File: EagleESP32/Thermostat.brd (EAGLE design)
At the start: 42.2 x 49.3 mm, 61 parts, among them K1 AQY282EHA, K2 AQY282EHA, K3 AQY282EHA, K4 AQY282EHA, K5 AQY282EHA, Q1 MOSFET-NCHANNELAO3404A, U1 ESP-WROOM-03, X1 1751303

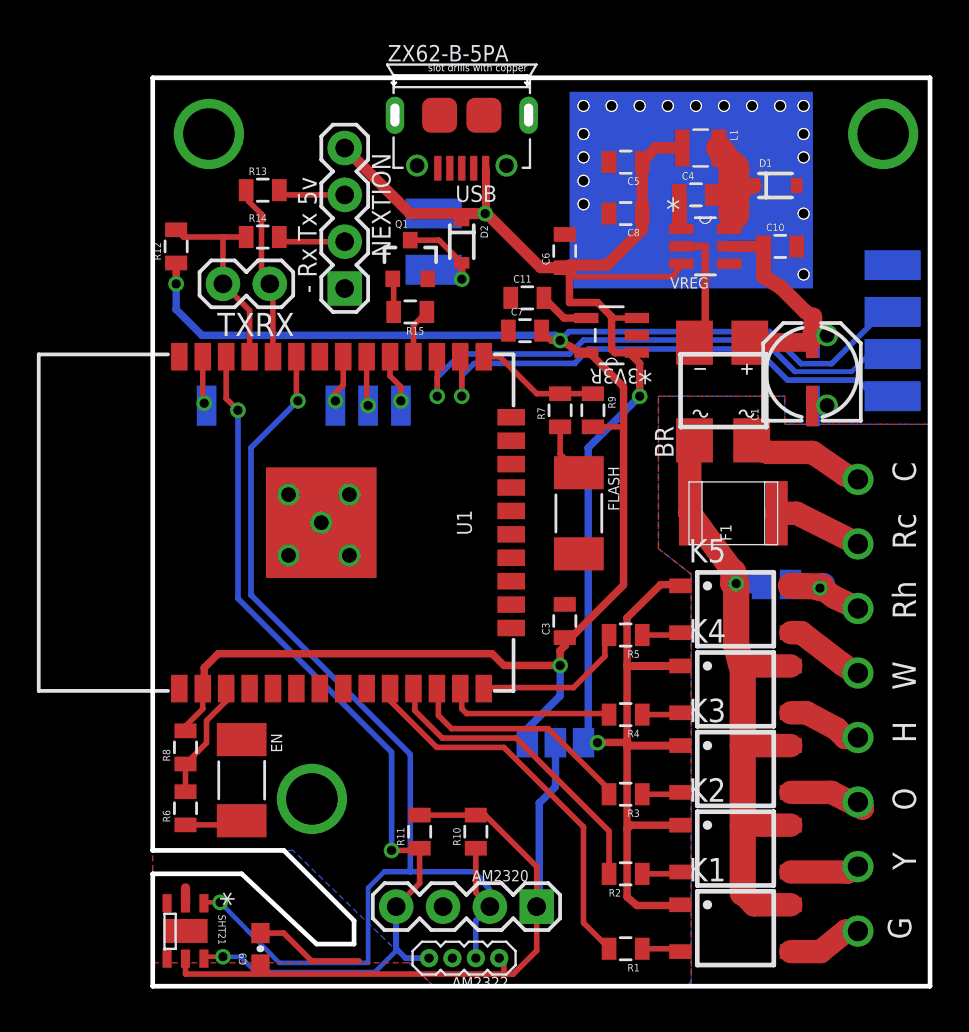
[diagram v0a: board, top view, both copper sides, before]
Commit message: rev 1. GPIO12 is connected to 1.3V LDO (r0 failed!)
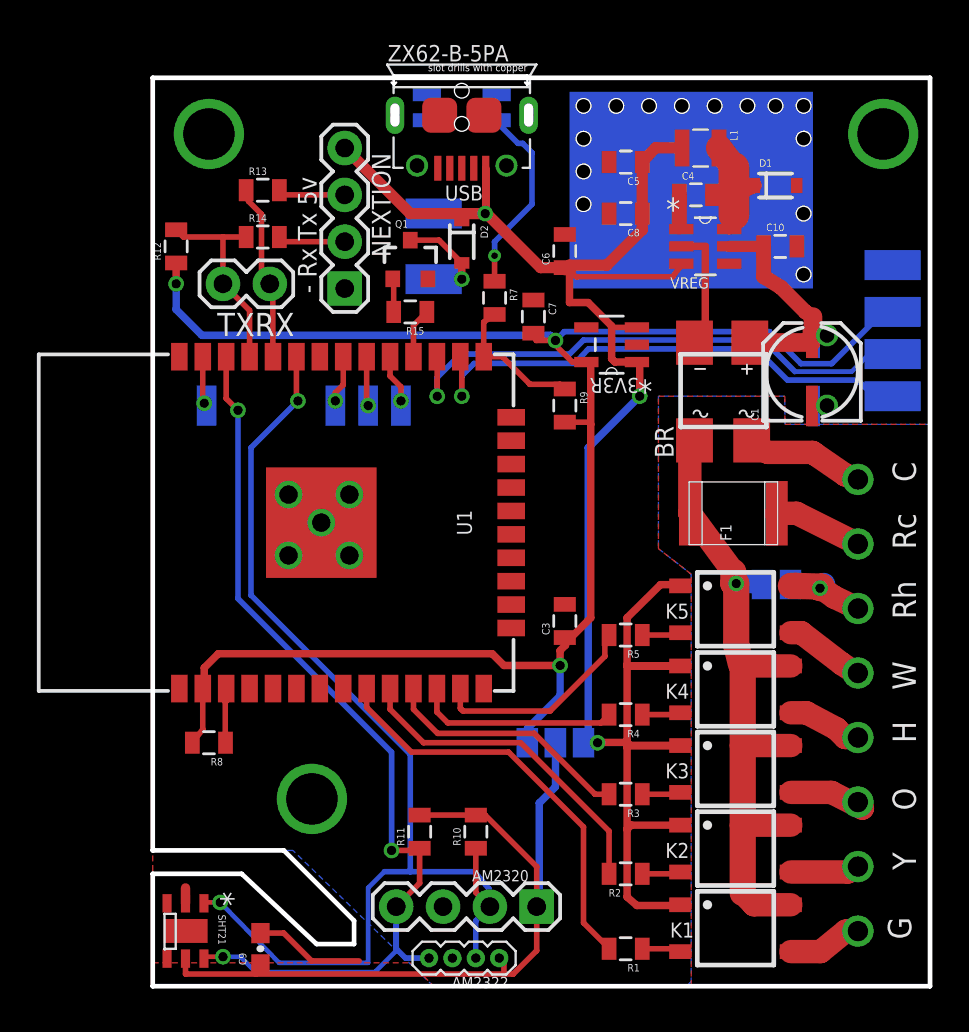
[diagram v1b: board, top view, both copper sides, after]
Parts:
- removed C11: (no value), SparkFun-Capacitors:0805
- removed EN, FLASH: BTN_4MM, CuriousTech:BTN_4MM
- removed R6: 470, SparkFun-Resistors:0805
- added U$6: SIDE-TACT, CuriousTech:SIDE-TACT
- K1, K2, K3, K4, K5: value AQY282EHA -> G3VM-61GR2
- moved R7 7.06 mm to (18.5, 37.3), turned to 270 degrees
- moved R9 1.55 mm to (22.4, 31.5)
- moved R8 1.30 mm to (3.05, 13.2), turned to 180 degrees
- moved C7 0.89 mm to (20.7, 36.3), turned to 270 degrees
- moved U$11 0.51 mm to (15.2, 38.4)
- moved 3V3R 0.51 mm to (24.9, 34.8)
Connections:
- removed net N$28: EN.2, R6.1
- removed net N$34: 3V3R.4, C11.2
- new net N$35: U1.24
- new net N$36: U1.16
- new net N$37: U1.23
- new net N$40: U1.8
- new net N$42: U1.6
- new net N$43: U1.7
- new net _NC: U1.32
- net COOL: now also U1.10; no longer U1.11
- net FAN: now also U1.9; no longer U1.10
- net GND: now also U$6.3, U$6.4; no longer C11.1, EN.1, FLASH.2
- net HEAT: now also U1.13; no longer U1.14
- net HUMID: now also U1.12; no longer U1.13
- net N$27: now also U$6.2; no longer FLASH.1
- net N$9: no longer R6.2
- net REV: now also U1.11; no longer U1.12
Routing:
- net N$27: track 2.91 -> 10.5 mm, vias 0 -> 1
- net N$9: track 6.51 -> 2.97 mm
- net N$28: track 3.14 -> 0.00 mm
- net HEAT: track 8.54 -> 11.5 mm
- net N$34: track 2.75 -> 0.00 mm
- net HUMID: track 9.25 -> 11.0 mm
- net FAN: track 21.2 -> 22.6 mm
- net COOL: track 16.8 -> 18.1 mm
- net N$14: track 6.75 -> 7.73 mm
- net REV: track 12.7 -> 13.6 mm
- net 5V: track 113.3 -> 112.6 mm
- net 3V3: track 96.9 -> 96.2 mm

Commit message: Worst mistake ever. I quit.
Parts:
- removed C2: 100uF, SparkFun-Capacitors:PANASONIC_C
- R14: value 5K6 -> 5K1
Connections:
- net 3V3: now also K1.1, K2.1, K3.1, K4.1, K5.1
- net 5V: no longer K1.1, K2.1, K3.1, K4.1, K5.1
- net GND: no longer C2.-
- net N$24: no longer C2.+
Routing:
- net 5V: track 112.6 -> 74.0 mm, vias 3 -> 2
- net 3V3: track 96.2 -> 129.7 mm
- net N$24: track 13.5 -> 12.7 mm
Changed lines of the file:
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@@
 <attribute name="VALUE" x="30.353" y="38.8874" size="2.0828" layer="27" ratio="10" rot="SR180"/>
 </element>
-<element name="R14" library="SparkFun-Resistors" package="0805" value="5K6" x="5.969" y="40.64" smashed="yes">
+<element name="R14" library="SparkFun-Resistors" package="0805" value="5K1" x="5.969" y="40.64" smashed="yes">
 <attribute name="NAME" x="5.207" y="41.4655" size="0.4064" layer="25"/>
 <attribute name="VALUE" x="4.953" y="39.243" size="0.4064" layer="27"/>
@@
 <attribute name="NAME" x="27.239" y="30.387" size="1.016" layer="25" ratio="10" rot="R270"/>
 <attribute name="VALUE" x="25.803" y="36.733" size="1.778" layer="27" ratio="10" rot="R270"/>
-</element>
-<element name="C2" library="SparkFun-Capacitors" package="PANASONIC_C" value="100uF" x="36.068" y="33.274" smashed="yes" rot="MR90">
-<attribute name="NAME" x="38.768" y="30.674" size="0.4064" layer="26" rot="MR90"/>
-<attribute name="VALUE" x="32.618" y="30.674" size="0.4064" layer="28" rot="MR90"/>
 </element>
 <element name="AM2320" library="SparkFun-Connectors" package="1X04" value="AM2320" x="20.828" y="4.318" smashed="yes" rot="R180">
@@
 <contactref element="C6" pad="2"/>
 <contactref element="BR" pad="-"/>
-<contactref element="C2" pad="-"/>
 <via x="36.576" y="31.496" extent="1-16" drill="0.8"/>
 <contactref element="AM2320" pad="3"/>
@@
 <wire x1="35.814" y1="36.322" x2="35.414178125" y2="36.570134375" width="0.8128" layer="1"/>
 <wire x1="35.414178125" y1="36.570134375" x2="34.07518125" y2="37.90913125" width="0.8128" layer="1"/>
-<contactref element="C2" pad="+"/>
 <wire x1="34.07518125" y1="37.90913125" x2="33.136" y2="38.492" width="0.8128" layer="1"/>
-<wire x1="36.576" y1="35.306" x2="36.444" y2="35.174" width="0.4064" layer="16"/>
-<wire x1="35.868" y1="35.174" x2="36.444" y2="35.174" width="0.4064" layer="16"/>
 <via x="36.576" y="35.306" extent="1-16" drill="0.8"/>
 <wire x1="36.576" y1="35.306" x2="36.4852875" y2="35.5781375" width="0.4064" layer="1"/>
@@
 <wire x1="22.352" y1="18.912" x2="22.393046875" y2="18.870953125" width="0.4064" layer="1"/>
 <wire x1="22.393046875" y1="18.870953125" x2="22.393046875" y2="18.500953125" width="0.4064" layer="1"/>
-<wire x1="23.76" y1="19.98230625" x2="23.76" y2="30.48" width="0.4064" layer="1"/>
+<wire x1="23.76" y1="19.98230625" x2="23.76" y2="20.447" width="0.4064" layer="1"/>
 <wire x1="23.76" y1="30.48" x2="23.76" y2="33.782" width="0.4064" layer="1"/>
 <wire x1="22.324846875" y1="35.5092" x2="21.84543125" y2="35.029784375" width="0.3048" layer="16"/>
@@
 <wire x1="23.5204" y1="33.8582" x2="22.760153125" y2="33.8582" width="0.3048" layer="1"/>
 <wire x1="22.760153125" y1="33.8582" x2="21.59" y2="35.028353125" width="0.3048" layer="1"/>
+<contactref element="K5" pad="1"/>
+<contactref element="K4" pad="1"/>
+<contactref element="K3" pad="1"/>
+<contactref element="K2" pad="1"/>
+<contactref element="K1" pad="1"/>
+<wire x1="26.26070625" y1="4.3784" x2="25.7302" y2="4.84070625" width="0.4064" layer="1"/>
+<wire x1="28.614" y1="4.418" x2="28.5744" y2="4.3784" width="0.4064" layer="1"/>
+<wire x1="28.5744" y1="4.3784" x2="26.26070625" y2="4.3784" width="0.4064" layer="1"/>
+<wire x1="25.7302" y1="4.84070625" x2="25.7302" y2="8.5138875" width="0.4064" layer="1"/>
+<wire x1="25.9523125" y1="8.736" x2="25.7302" y2="8.5138875" width="0.4064" layer="1"/>
+<wire x1="28.614" y1="8.736" x2="25.9523125" y2="8.736" width="0.4064" layer="1"/>
+<wire x1="28.614" y1="13.054" x2="28.514" y2="12.954" width="0.4064" layer="1"/>
+<wire x1="28.514" y1="12.954" x2="25.908" y2="12.954" width="0.4064" layer="1"/>
+<wire x1="25.908" y1="12.954" x2="25.7302" y2="12.7762" width="0.4064" layer="1"/>
+<wire x1="25.7302" y1="12.7762" x2="25.7302" y2="12.446" width="0.4064" layer="1"/>
+<wire x1="25.7302" y1="12.446" x2="25.7302" y2="8.5138875" width="0.4064" layer="1"/>
+<wire x1="28.614" y1="17.372" x2="28.514" y2="17.272" width="0.4064" layer="1"/>
+<wire x1="28.514" y1="17.272" x2="25.654" y2="17.272" width="0.4064" layer="1"/>
+<wire x1="25.654" y1="17.272" x2="25.654" y2="12.5222" width="0.4064" layer="1"/>
+<wire x1="25.654" y1="12.5222" x2="25.7302" y2="12.446" width="0.4064" layer="1"/>
+<wire x1="28.614" y1="21.717" x2="27.051" y2="21.717" width="0.4064" layer="1"/>
+<wire x1="27.051" y1="21.717" x2="25.781" y2="20.447" width="0.4064" layer="1"/>
+<wire x1="25.781" y1="20.447" x2="25.654" y2="20.32" width="0.4064" layer="1"/>
+<wire x1="25.654" y1="20.32" x2="25.654" y2="17.272" width="0.4064" layer="1"/>
+<wire x1="23.76" y1="20.447" x2="25.781" y2="20.447" width="0.4064" layer="1"/>
+<wire x1="23.76" y1="30.48" x2="23.76" y2="20.447" width="0.4064" layer="1"/>
 </signal>
 <signal name="TXD">
@@
 <contactref element="U$5" pad="&gt;PAD"/>
 <contactref element="D2" pad="C"/>
-<contactref element="K1" pad="1"/>
-<contactref element="K2" pad="1"/>
-<contactref element="K3" pad="1"/>
-<contactref element="K4" pad="1"/>
-<contactref element="K5" pad="1"/>
-<wire x1="26.26070625" y1="4.3784" x2="25.7302" y2="4.84070625" width="0.4064" layer="1"/>
-<wire x1="25.9523125" y1="8.736" x2="28.614" y2="8.736" width="0.4064" layer="1"/>
-<wire x1="28.614" y1="4.418" x2="28.5744" y2="4.3784" width="0.4064" layer="1"/>
-<wire x1="28.5744" y1="4.3784" x2="26.26070625" y2="4.3784" width="0.4064" layer="1"/>
-<wire x1="28.614" y1="21.717" x2="28.5474" y2="21.7836" width="0.4064" layer="1"/>
-<wire x1="28.5474" y1="21.7836" x2="27.5494125" y2="21.7836" width="0.4064" layer="1"/>
-<wire x1="27.5494125" y1="21.7836" x2="25.7302" y2="19.986446875" width="0.4064" layer="1"/>
-<wire x1="25.7302" y1="17.44309375" x2="25.7302" y2="19.986446875" width="0.4064" layer="1"/>
-<via x="24.13" y="13.208" extent="1-16" drill="0.5"/>
-<wire x1="24.13" y1="13.208" x2="23.368" y2="13.208" width="0.4064" layer="16"/>
-<wire x1="28.614" y1="17.372" x2="25.7302" y2="17.372" width="0.4064" layer="1"/>
-<wire x1="28.614" y1="17.372" x2="25.80129375" y2="17.372" width="0.4064" layer="1"/>
-<wire x1="25.80129375" y1="17.372" x2="25.7302" y2="17.44309375" width="0.4064" layer="1"/>
-<wire x1="28.614" y1="13.054" x2="25.8302" y2="13.054" width="0.4064" layer="1"/>
-<wire x1="25.733553125" y1="13.226059375" x2="24.148059375" y2="13.226059375" width="0.4064" layer="1"/>
-<wire x1="24.13" y1="13.208" x2="24.148059375" y2="13.226059375" width="0.4064" layer="1"/>
-<wire x1="25.7302" y1="4.84070625" x2="25.7302" y2="8.5138875" width="0.4064" layer="1"/>
-<wire x1="25.7302" y1="8.5138875" x2="25.9523125" y2="8.736" width="0.4064" layer="1"/>
-<wire x1="25.8302" y1="13.054" x2="25.7302" y2="12.954" width="0.4064" layer="1"/>
-<wire x1="25.7302" y1="12.954" x2="25.7302" y2="8.5138875" width="0.4064" layer="1"/>
-<wire x1="25.7302" y1="13.29090625" x2="25.733553125" y2="13.226059375" width="0.4064" layer="1"/>
-<wire x1="25.7302" y1="17.372" x2="25.7302" y2="13.29090625" width="0.4064" layer="1"/>
-<wire x1="28.614" y1="13.054" x2="25.9056125" y2="13.054" width="0.4064" layer="1"/>
-<wire x1="25.9056125" y1="13.054" x2="25.733553125" y2="13.226059375" width="0.4064" layer="1"/>
-<wire x1="25.7302" y1="17.44309375" x2="25.7302" y2="17.372" width="0.4064" layer="1"/>
 <wire x1="16.764" y1="41.536" x2="16.764" y2="41.91" width="0.3048" layer="1"/>
 <wire x1="15.24" y1="41.91" x2="18.034" y2="41.91" width="0.4064" layer="16"/>
